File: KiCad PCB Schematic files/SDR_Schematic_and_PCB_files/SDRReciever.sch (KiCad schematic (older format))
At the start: 62 parts, among them J1 Conn_Coaxial, J10 I_0, J11 I_180, J12 Q_90, J13 Q_270, J14 AudioJack3, J2 3.3V, J3 FIL_IN, J4 5V, J5 4.3V, J6 FIL_OUT, J7 CLK_2, J8 CLK_0, J9 CLK_1, Q1 MMBT2222A-TP, Q2 BSS138, Q3 BSS138, U1 Si5351A-B-GT, U2 SN74CBT3253, U3 LM4562, Y1 CX3225SB

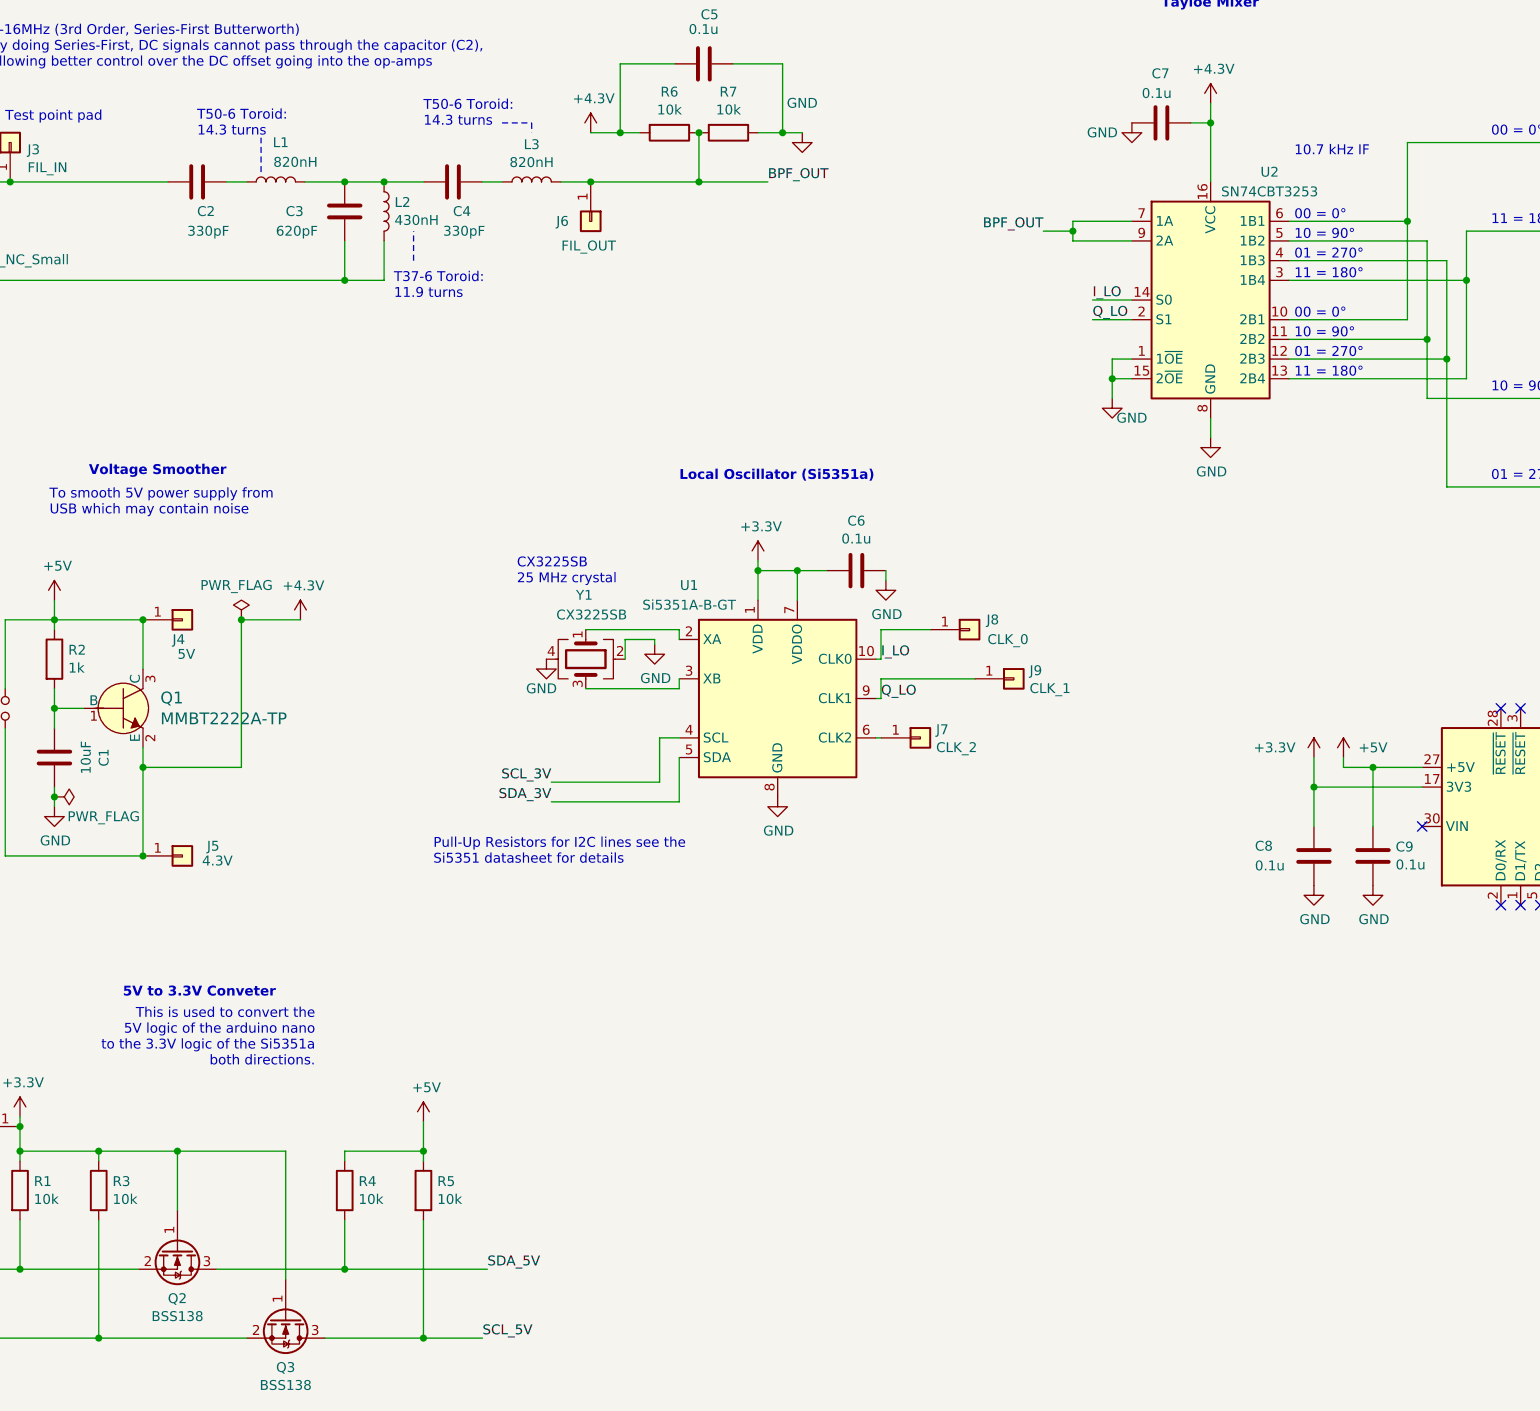
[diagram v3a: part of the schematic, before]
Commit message: Initial PCB part layout complete Trace not routed yet
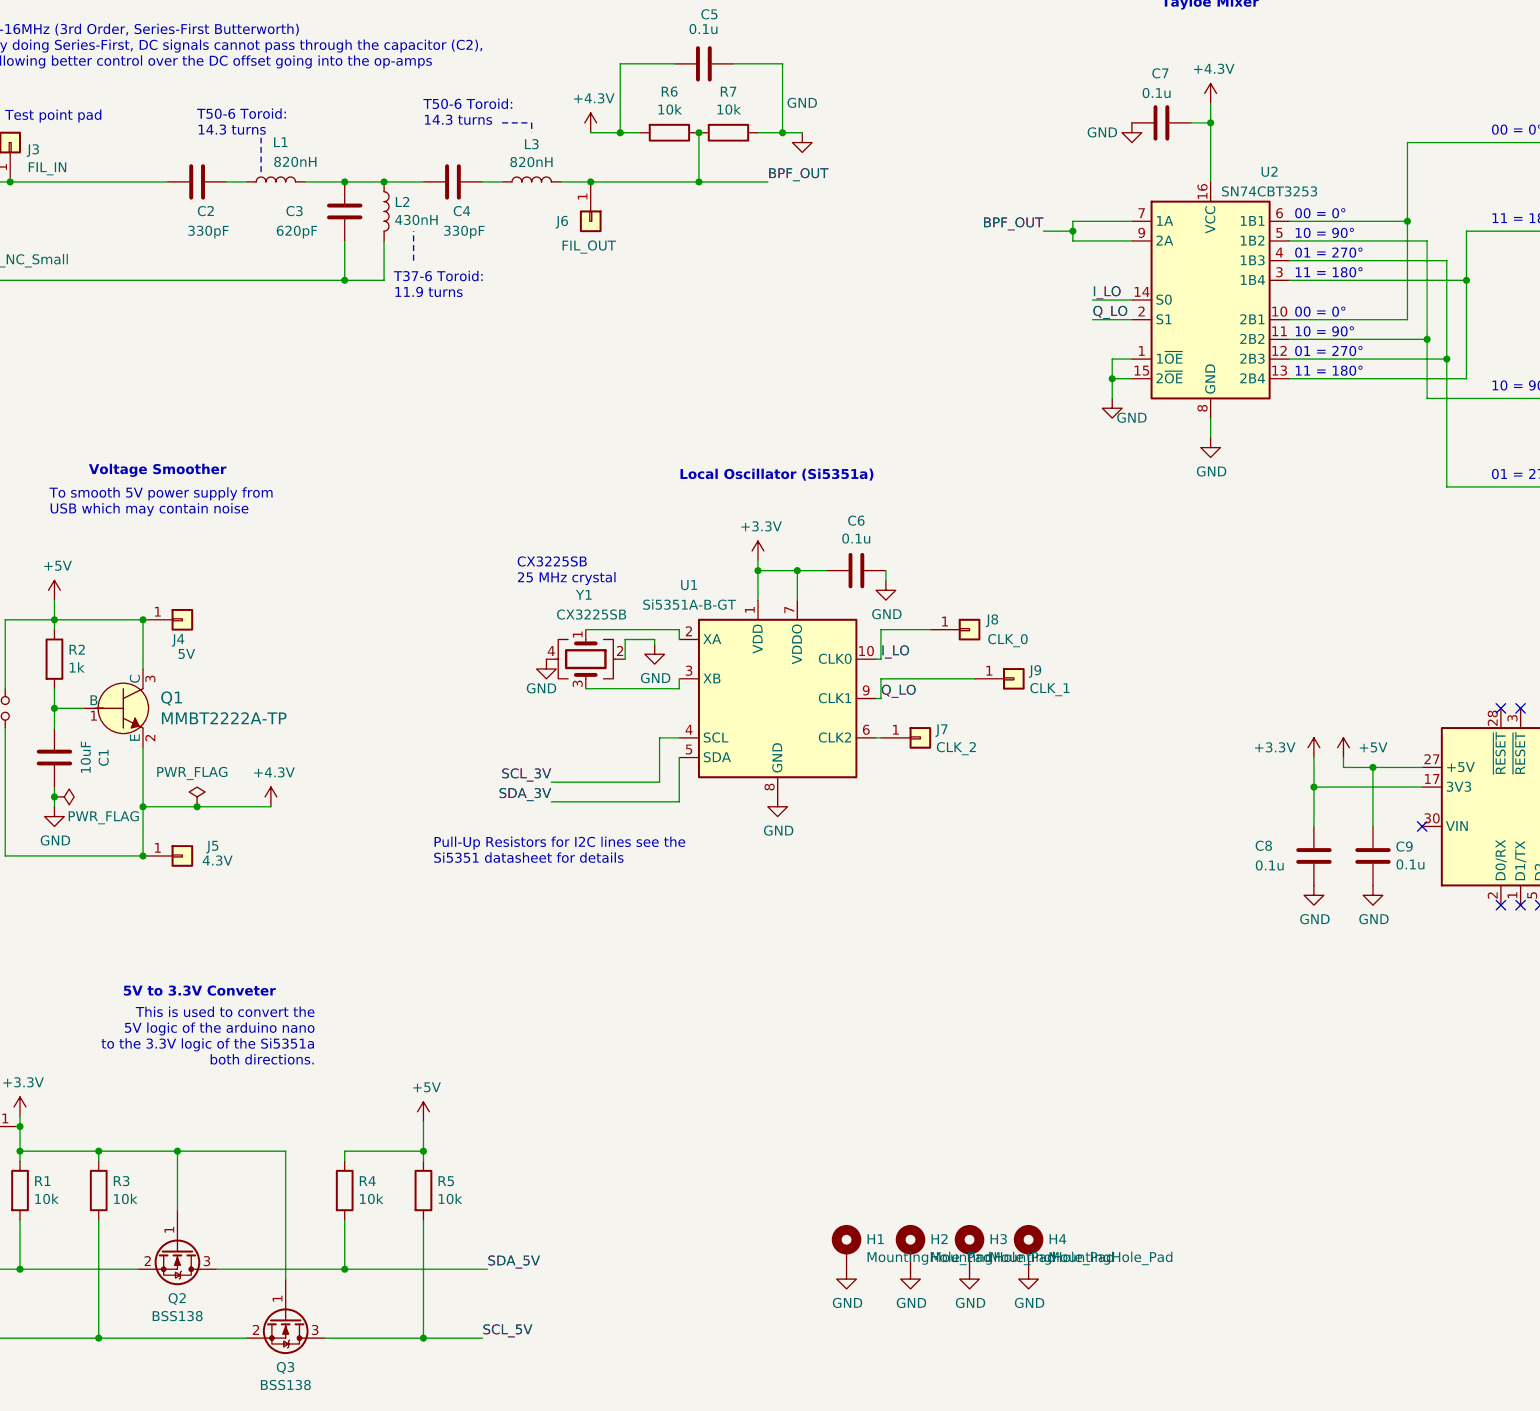
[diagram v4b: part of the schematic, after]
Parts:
- added H1, H2, H3, H4: MountingHole_Pad, MountingHole:MountingHole_2.2mm_M2_Pad, symbol Mechanical:MountingHole_Pad
- J1: footprint Connector_TE-Connectivity:BNC_Socket_TYCO-AMP_LargePads -> Connector_Coaxial:BNC_Amphenol_B6252HB-NPP3G-50_Horizontal
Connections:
- net GND: now also H1.1, H2.1, H3.1, H4.1
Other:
- note removed: "10.7 kHz IF"
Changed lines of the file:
@@
 Comp "Walla Walla University"
 Comment1 "Author: Caleb Nelson"
-Comment2 ""
-Comment3 "ENGR 357"
+Comment2 "ENGR 357"
+Comment3 ""
 Comment4 ""
 $EndDescr
@@
 Wire Wire Line
 	5750 4475 5750 4425
-Text Notes 8875 1775 0    50   ~ 0
-10.7 kHz IF
 $Comp
 L SDRReciever-rescue:GND-power-SDRReciever-rescue #PWR011
@@
 F 0 "J1" H 2350 2100 50  0000 C CNN
 F 1 "Conn_Coaxial" H 2350 2000 50  0000 C CNN
-F 2 "Connector_TE-Connectivity:BNC_Socket_TYCO-AMP_LargePads" H 2000 1900 50  0001 C CNN
+F 2 "Connector_Coaxial:BNC_Amphenol_B6252HB-NPP3G-50_Horizontal" H 2000 1900 50  0001 C CNN
 F 3 " ~" H 2000 1900 50  0001 C CNN
 	1    2000 1900
@@
 	2325 4675 2325 5325
 Wire Wire Line
-	3025 5325 3025 4875
-Connection ~ 3025 4875
-Wire Wire Line
-	3025 4875 3025 4775
+	3025 5325 3025 5075
+Connection ~ 3025 5075
+Wire Wire Line
+	3025 5075 3025 4775
 Connection ~ 2575 5025
 Wire Wire Line
@@
 L 4V3Power:+4.3V #PWR05
 U 1 1 5F3E7A8D
-P 3825 4125
-F 0 "#PWR05" H 3825 3975 50  0001 C CNN
-F 1 "+4.3V" H 3840 4298 50  0000 C CNN
-F 2 "" H 3825 4125 50  0001 C CNN
-F 3 "" H 3825 4125 50  0001 C CNN
-	1    3825 4125
+P 3675 5075
+F 0 "#PWR05" H 3675 4925 50  0001 C CNN
+F 1 "+4.3V" H 3690 5248 50  0000 C CNN
+F 2 "" H 3675 5075 50  0001 C CNN
+F 3 "" H 3675 5075 50  0001 C CNN
+	1    3675 5075
 	1    0    0    -1
 $EndComp
@@
 L SDRReciever-rescue:PWR_FLAG-power-SDRReciever-rescue #FLG02
 U 1 1 5F3E8DB4
-P 3525 4125
-F 0 "#FLG02" H 3525 4200 50  0001 C CNN
-F 1 "PWR_FLAG" H 3500 4300 50  0000 C CNN
-F 2 "" H 3525 4125 50  0001 C CNN
-F 3 "~" H 3525 4125 50  0001 C CNN
-	1    3525 4125
+P 3300 5075
+F 0 "#FLG02" H 3300 5150 50  0001 C CNN
+F 1 "PWR_FLAG" H 3275 5250 50  0000 C CNN
+F 2 "" H 3300 5075 50  0001 C CNN
+F 3 "~" H 3300 5075 50  0001 C CNN
+	1    3300 5075
 	1    0    0    -1
 $EndComp
@@
 $EndComp
 Wire Wire Line
-	3525 4125 3825 4125
+	3300 5075 3675 5075
 Wire Wire Line
 	2325 4125 2575 4125
@@
 Connection ~ 3025 5325
 Wire Wire Line
-	3525 4875 3525 4125
-Wire Wire Line
-	3025 4875 3525 4875
+	3025 5075 3300 5075
 Text Notes 1425 4300 0    50   ~ 0
 Voltage Smoother \nFor PC 5V power to \neliminate supply noise
@@
 Text Notes 4500 5375 0    50   ~ 0
 Pull-Up Resistors for I2C lines see the \nSi5351 datasheet for details
-Connection ~ 3525 4125
+Connection ~ 3300 5075
 Text Notes 11100 4500 0    50   ~ 0
 SDA and SCL are I2C Control Signals \nfor the Si5351 Clock Generator
@@
 	1    0    0    -1
 $EndComp
+$Comp
+L Mechanical:MountingHole_Pad H1
+U 1 1 608BA5A4
+P 6600 7325
+F 0 "H1" H 6700 7376 50  0000 L CNN
+F 1 "MountingHole_Pad" H 6700 7285 50  0000 L CNN
+F 2 "MountingHole:MountingHole_2.2mm_M2_Pad" H 6600 7325 50  0001 C CNN
+F 3 "~" H 6600 7325 50  0001 C CNN
+	1    6600 7325
+	1    0    0    -1
+$EndComp
+$Comp
+L SDRReciever-rescue:GND-power-SDRReciever-rescue #PWR030
+U 1 1 608BA936
+P 6600 7425
+F 0 "#PWR030" H 6600 7175 50  0001 C CNN
+F 1 "GND" H 6605 7252 50  0000 C CNN
+F 2 "" H 6600 7425 50  0001 C CNN
+F 3 "" H 6600 7425 50  0001 C CNN
+	1    6600 7425
+	1    0    0    -1
+$EndComp
+$Comp
+L Mechanical:MountingHole_Pad H2
+U 1 1 608BAB46
+P 6925 7325
+F 0 "H2" H 7025 7376 50  0000 L CNN
+F 1 "MountingHole_Pad" H 7025 7285 50  0000 L CNN
+F 2 "MountingHole:MountingHole_2.2mm_M2_Pad" H 6925 7325 50  0001 C CNN
+F 3 "~" H 6925 7325 50  0001 C CNN
+	1    6925 7325
+	1    0    0    -1
+$EndComp
+$Comp
+L SDRReciever-rescue:GND-power-SDRReciever-rescue #PWR031
+U 1 1 608BAB4D
+P 6925 7425
+F 0 "#PWR031" H 6925 7175 50  0001 C CNN
+F 1 "GND" H 6930 7252 50  0000 C CNN
+F 2 "" H 6925 7425 50  0001 C CNN
+F 3 "" H 6925 7425 50  0001 C CNN
+	1    6925 7425
+	1    0    0    -1
+$EndComp
+$Comp
+L Mechanical:MountingHole_Pad H3
+U 1 1 608C3728
+P 7225 7325
+F 0 "H3" H 7325 7376 50  0000 L CNN
+F 1 "MountingHole_Pad" H 7325 7285 50  0000 L CNN
+F 2 "MountingHole:MountingHole_2.2mm_M2_Pad" H 7225 7325 50  0001 C CNN
+F 3 "~" H 7225 7325 50  0001 C CNN
+	1    7225 7325
+	1    0    0    -1
+$EndComp
+$Comp
+L SDRReciever-rescue:GND-power-SDRReciever-rescue #PWR032
+U 1 1 608C372F
+P 7225 7425
+F 0 "#PWR032" H 7225 7175 50  0001 C CNN
+F 1 "GND" H 7230 7252 50  0000 C CNN
+F 2 "" H 7225 7425 50  0001 C CNN
+F 3 "" H 7225 7425 50  0001 C CNN
+	1    7225 7425
+	1    0    0    -1
+$EndComp
+$Comp
+L Mechanical:MountingHole_Pad H4
+U 1 1 608CC30B
+P 7525 7325
+F 0 "H4" H 7625 7376 50  0000 L CNN
+F 1 "MountingHole_Pad" H 7625 7285 50  0000 L CNN
+F 2 "MountingHole:MountingHole_2.2mm_M2_Pad" H 7525 7325 50  0001 C CNN
+F 3 "~" H 7525 7325 50  0001 C CNN
+	1    7525 7325
+	1    0    0    -1
+$EndComp
+$Comp
+L SDRReciever-rescue:GND-power-SDRReciever-rescue #PWR033
+U 1 1 608CC312
+P 7525 7425
+F 0 "#PWR033" H 7525 7175 50  0001 C CNN
+F 1 "GND" H 7530 7252 50  0000 C CNN
+F 2 "" H 7525 7425 50  0001 C CNN
+F 3 "" H 7525 7425 50  0001 C CNN
+	1    7525 7425
+	1    0    0    -1
+$EndComp

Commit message: Revised placement of PCB parts
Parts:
- H1, H2, H3, H4: symbol Mechanical:MountingHole_Pad -> SDRReciever-rescue:MountingHole_Pad-Mechanical
- J14: symbol 35RAPC4BHN2:35RAPC4BHN2 -> SDRReciever-rescue:35RAPC4BHN2-35RAPC4BHN2
- Q1: symbol dk_Transistors-Bipolar-BJT-Single:MMBT2222A-TP -> SDRReciever-rescue:MMBT2222A-TP-dk_Transistors-Bipolar-BJT-Single
- Q2, Q3: symbol Device:Q_NMOS_GSD -> SDRReciever-rescue:Q_NMOS_GSD-Device
- Y1: symbol Device:Crystal_GND24 -> SDRReciever-rescue:Crystal_GND24-Device
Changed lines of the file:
@@
 EESchema Schematic File Version 4
-LIBS:SDRReciever-cache
-EELAYER 26 0
+EELAYER 30 0
 EELAYER END
 $Descr A3 16535 11693
@@
 $EndComp
 $Comp
-L 35RAPC4BHN2:35RAPC4BHN2 J14
+L SDRReciever-rescue:35RAPC4BHN2-35RAPC4BHN2 J14
 U 1 1 5E956DCB
 P 15300 2650
@@
 $EndComp
 $Comp
-L Device:Crystal_GND24 Y1
+L SDRReciever-rescue:Crystal_GND24-Device Y1
 U 1 1 5EA4F383
 P 5275 4325
@@
 Connection ~ 4450 6825
 $Comp
-L Device:Q_NMOS_GSD Q2
+L SDRReciever-rescue:Q_NMOS_GSD-Device Q2
 U 1 1 608B7971
 P 3200 7325
@@
 	4450 7775 3950 7775
 $Comp
-L Device:Q_NMOS_GSD Q3
+L SDRReciever-rescue:Q_NMOS_GSD-Device Q3
 U 1 1 608C951F
 P 3750 7675
@@
 NoConn ~ 15000 2650
 $Comp
-L dk_Transistors-Bipolar-BJT-Single:MMBT2222A-TP Q1
+L SDRReciever-rescue:MMBT2222A-TP-dk_Transistors-Bipolar-BJT-Single Q1
 U 1 1 608B107C
 P 2925 4575
@@
 $EndComp
 $Comp
-L Mechanical:MountingHole_Pad H1
+L SDRReciever-rescue:MountingHole_Pad-Mechanical H1
 U 1 1 608BA5A4
 P 6600 7325
@@
 $EndComp
 $Comp
-L Mechanical:MountingHole_Pad H2
+L SDRReciever-rescue:MountingHole_Pad-Mechanical H2
 U 1 1 608BAB46
 P 6925 7325
@@
 $EndComp
 $Comp
-L Mechanical:MountingHole_Pad H3
+L SDRReciever-rescue:MountingHole_Pad-Mechanical H3
 U 1 1 608C3728
 P 7225 7325
@@
 $EndComp
 $Comp
-L Mechanical:MountingHole_Pad H4
+L SDRReciever-rescue:MountingHole_Pad-Mechanical H4
 U 1 1 608CC30B
 P 7525 7325
